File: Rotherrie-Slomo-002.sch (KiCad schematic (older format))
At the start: 8 parts, among them U2 TL074

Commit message: Oscillator section done
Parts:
- added C12, C17, C20: 100uF, symbol CP
- added C14, C16, C18, C19, C21, C22: 100nF, symbol C
- added R10, R11, R13, R14, R16, R6: 4.7k, symbol R
- added R12, R15, R8: 100k, symbol R
- added RV2, RV3, RV4: 500k, symbol POT
- added unit 3 of U2
- added unit 4 of U2
- added unit 2 of U2
- gave numbers to parts that had none: 7
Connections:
- net GND: now also C12.2, C14.1, C16.1, C17.2, C18.1, C19.1, C20.2, C21.1, C22.1, R11.2, R14.2, R6.2
- net VCC: now also C14.2, C18.2, C21.2, U2.4 (V+), U2.4 (V+), U2.4 (V+)
- net VEE: now also C16.2, C19.2, C22.2, U2.11 (V-), U2.11 (V-), U2.11 (V-)
- new net: R11.1, R13.2, U2.10 (+)
- new net: R13.1, U2.8
- new net: C17.1, R12.1, U2.9 (-)
- new net: R12.2, RV3.2, RV3.3
- new net: R14.1, R16.2, U2.12 (+)
- new net: C20.1, R15.1, U2.13 (-)
- new net: R16.1, U2.14
- new net: R15.2, RV4.2, RV4.3
- new net: R10.2, R6.1, U2.5 (+)
- new net: C12.1, R8.1, U2.6 (-)
- new net: R10.1, U2.7
- new net: R8.2, RV2.2, RV2.3
- new net WAVE2: RV3.1
- new net WAVE3: RV4.1
- new net WAVE4: RV2.1
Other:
- moved on the sheet: C11, C13, C15, R5, R7, R9, RV1, U2A

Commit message: Part associations made. 16pin connector reduced to 10 pin
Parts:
- removed C14, C16, C18, C19, C21, C22: 100nF, symbol C
- C10: renamed from C20; footprint (none) -> Capacitors_THT:CP_Radial_D7.5mm_P2.50mm
- C5: renamed from C11; footprint (none) -> Capacitors_THT:CP_Radial_D7.5mm_P2.50mm
- C6: renamed from C12; footprint (none) -> Capacitors_THT:CP_Radial_D7.5mm_P2.50mm
- C7: renamed from C13; footprint (none) -> Capacitors_THT:C_Disc_D4.3mm_W1.9mm_P5.00mm
- C8: renamed from C15; footprint (none) -> Capacitors_THT:C_Disc_D4.3mm_W1.9mm_P5.00mm
- C9: renamed from C17; footprint (none) -> Capacitors_THT:CP_Radial_D7.5mm_P2.50mm
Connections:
- net VCC: no longer U2.4 (V+), U2.4 (V+), U2.4 (V+)
- net VEE: no longer U2.11 (V-), U2.11 (V-), U2.11 (V-)
- net WAVE2: now also RV2.1; no longer RV3.1
- net WAVE3: now also RV3.1; no longer RV4.1
- net WAVE4: now also RV4.1; no longer RV2.1
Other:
- moved on the sheet: C6, R10, R6, R8, RV2, U2B

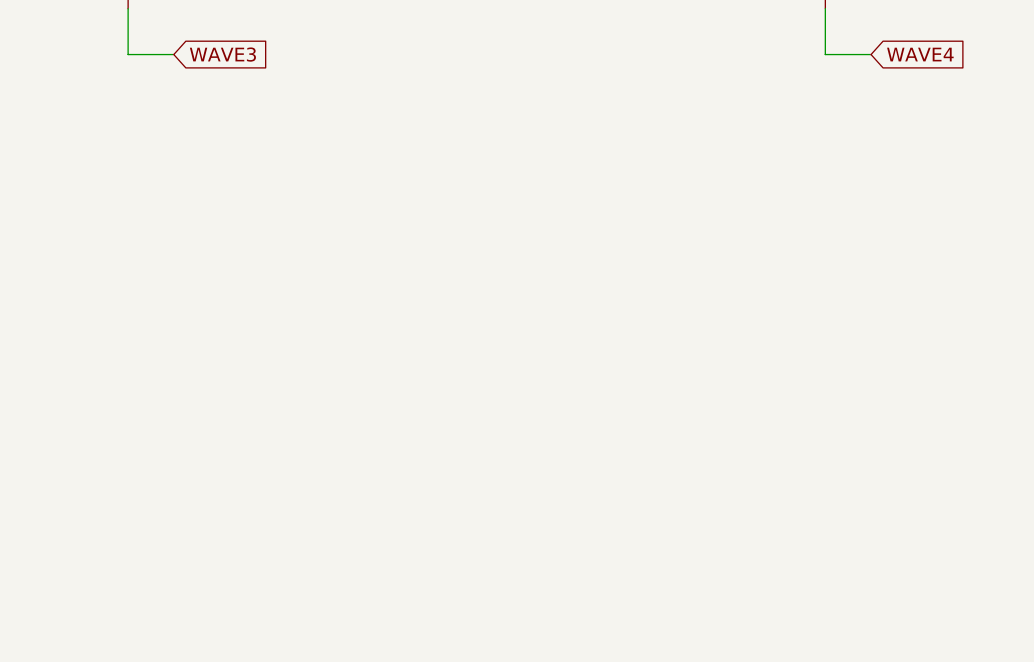
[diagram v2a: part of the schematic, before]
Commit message: Added jack connectors to schematic
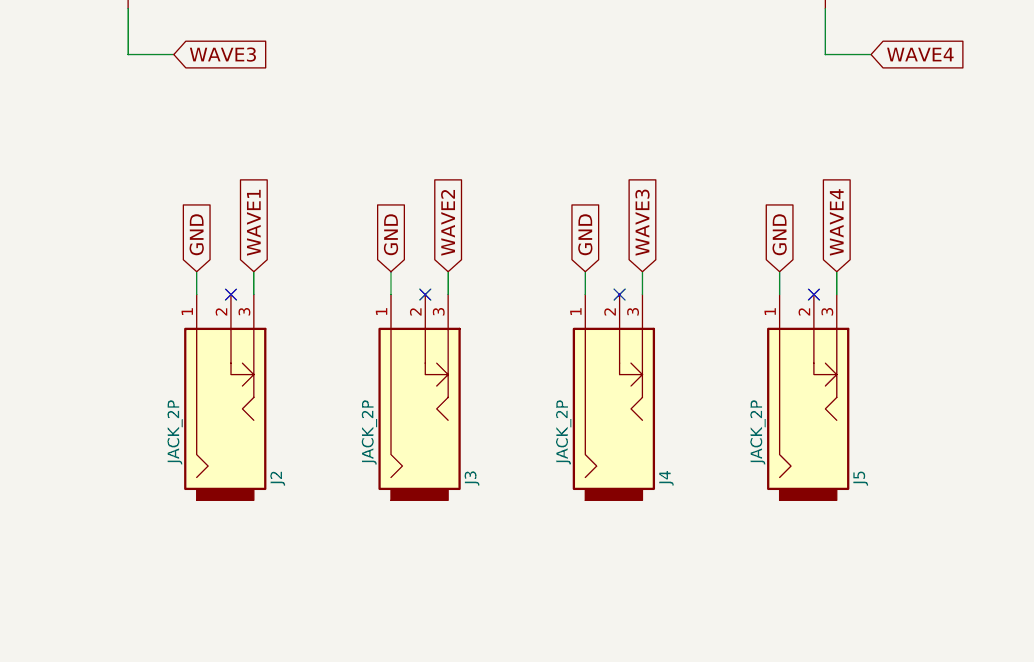
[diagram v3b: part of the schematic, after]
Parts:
- added J2, J3, J4, J5: JACK_2P, symbol JACK_2P
- R10, R11, R12, R13, R14, R15, R16, R5, R6, R7, R8, R9: footprint (none) -> Resistors_THT:R_Axial_DIN0207_L6.3mm_D2.5mm_P7.62mm_Horizontal
- RV1, RV2, RV3, RV4: footprint (none) -> Potentiometers:Potentiometer_Bourns_PTV09A-1_Horizontal
- U2: footprint (none) -> Housings_DIP:DIP-14_W7.62mm_Socket
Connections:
- net GND: now also J2.1, J3.1, J4.1, J5.1
- net WAVE1: now also J2.3
- net WAVE2: now also J3.3
- net WAVE3: now also J4.3
- net WAVE4: now also J5.3
- no-connect marks 0 -> 4
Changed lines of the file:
@@
 F 0 "U2" H 3350 2550 50  0000 L CNN
 F 1 "TL074" H 3350 2150 50  0000 L CNN
-F 2 "" H 3300 2450 50  0001 C CNN
+F 2 "Housings_DIP:DIP-14_W7.62mm_Socket" H 3300 2450 50  0001 C CNN
 F 3 "" H 3400 2550 50  0001 C CNN
 	1    3350 2350
@@
 F 0 "R9" V 3230 1350 50  0000 C CNN
 F 1 "4.7k" V 3150 1350 50  0000 C CNN
-F 2 "" V 3080 1350 50  0001 C CNN
+F 2 "Resistors_THT:R_Axial_DIN0207_L6.3mm_D2.5mm_P7.62mm_Horizontal" V 3080 1350 50  0001 C CNN
 F 3 "" H 3150 1350 50  0001 C CNN
 	1    3150 1350
@@
 F 0 "R5" V 2080 1350 50  0000 C CNN
 F 1 "4.7k" V 2000 1350 50  0000 C CNN
-F 2 "" V 1930 1350 50  0001 C CNN
+F 2 "Resistors_THT:R_Axial_DIN0207_L6.3mm_D2.5mm_P7.62mm_Horizontal" V 1930 1350 50  0001 C CNN
 F 3 "" H 2000 1350 50  0001 C CNN
 	1    2000 1350
@@
 F 0 "R7" V 2430 2900 50  0000 C CNN
 F 1 "100k" V 2350 2900 50  0000 C CNN
-F 2 "" V 2280 2900 50  0001 C CNN
+F 2 "Resistors_THT:R_Axial_DIN0207_L6.3mm_D2.5mm_P7.62mm_Horizontal" V 2280 2900 50  0001 C CNN
 F 3 "" H 2350 2900 50  0001 C CNN
 	1    2350 2900
@@
 F 0 "RV1" V 2325 3300 50  0000 C CNN
 F 1 "500k" V 2400 3300 50  0000 C CNN
-F 2 "" H 2500 3300 50  0001 C CNN
+F 2 "Potentiometers:Potentiometer_Bourns_PTV09A-1_Horizontal" H 2500 3300 50  0001 C CNN
 F 3 "" H 2500 3300 50  0001 C CNN
 	1    2500 3300
@@
 F 0 "U2" H 6400 2550 50  0000 L CNN
 F 1 "TL074" H 6400 2150 50  0000 L CNN
-F 2 "" H 6350 2450 50  0001 C CNN
+F 2 "Housings_DIP:DIP-14_W7.62mm_Socket" H 6350 2450 50  0001 C CNN
 F 3 "" H 6450 2550 50  0001 C CNN
 	3    6400 2350
@@
 F 0 "R13" V 6280 1350 50  0000 C CNN
 F 1 "4.7k" V 6200 1350 50  0000 C CNN
-F 2 "" V 6130 1350 50  0001 C CNN
+F 2 "Resistors_THT:R_Axial_DIN0207_L6.3mm_D2.5mm_P7.62mm_Horizontal" V 6130 1350 50  0001 C CNN
 F 3 "" H 6200 1350 50  0001 C CNN
 	1    6200 1350
@@
 F 0 "R11" V 5130 1350 50  0000 C CNN
 F 1 "4.7k" V 5050 1350 50  0000 C CNN
-F 2 "" V 4980 1350 50  0001 C CNN
+F 2 "Resistors_THT:R_Axial_DIN0207_L6.3mm_D2.5mm_P7.62mm_Horizontal" V 4980 1350 50  0001 C CNN
 F 3 "" H 5050 1350 50  0001 C CNN
 	1    5050 1350
@@
 F 0 "R12" V 5480 2900 50  0000 C CNN
 F 1 "100k" V 5400 2900 50  0000 C CNN
-F 2 "" V 5330 2900 50  0001 C CNN
+F 2 "Resistors_THT:R_Axial_DIN0207_L6.3mm_D2.5mm_P7.62mm_Horizontal" V 5330 2900 50  0001 C CNN
 F 3 "" H 5400 2900 50  0001 C CNN
 	1    5400 2900
@@
 F 0 "RV3" V 5375 3300 50  0000 C CNN
 F 1 "500k" V 5450 3300 50  0000 C CNN
-F 2 "" H 5550 3300 50  0001 C CNN
+F 2 "Potentiometers:Potentiometer_Bourns_PTV09A-1_Horizontal" H 5550 3300 50  0001 C CNN
 F 3 "" H 5550 3300 50  0001 C CNN
 	1    5550 3300
@@
 F 0 "U2" H 9450 2550 50  0000 L CNN
 F 1 "TL074" H 9450 2150 50  0000 L CNN
-F 2 "" H 9400 2450 50  0001 C CNN
+F 2 "Housings_DIP:DIP-14_W7.62mm_Socket" H 9400 2450 50  0001 C CNN
 F 3 "" H 9500 2550 50  0001 C CNN
 	4    9450 2350
@@
 F 0 "R16" V 9330 1350 50  0000 C CNN
 F 1 "4.7k" V 9250 1350 50  0000 C CNN
-F 2 "" V 9180 1350 50  0001 C CNN
+F 2 "Resistors_THT:R_Axial_DIN0207_L6.3mm_D2.5mm_P7.62mm_Horizontal" V 9180 1350 50  0001 C CNN
 F 3 "" H 9250 1350 50  0001 C CNN
 	1    9250 1350
@@
 F 0 "R14" V 8180 1350 50  0000 C CNN
 F 1 "4.7k" V 8100 1350 50  0000 C CNN
-F 2 "" V 8030 1350 50  0001 C CNN
+F 2 "Resistors_THT:R_Axial_DIN0207_L6.3mm_D2.5mm_P7.62mm_Horizontal" V 8030 1350 50  0001 C CNN
 F 3 "" H 8100 1350 50  0001 C CNN
 	1    8100 1350
@@
 F 0 "R15" V 8530 2900 50  0000 C CNN
 F 1 "100k" V 8450 2900 50  0000 C CNN
-F 2 "" V 8380 2900 50  0001 C CNN
+F 2 "Resistors_THT:R_Axial_DIN0207_L6.3mm_D2.5mm_P7.62mm_Horizontal" V 8380 2900 50  0001 C CNN
 F 3 "" H 8450 2900 50  0001 C CNN
 	1    8450 2900
@@
 F 0 "RV4" V 8425 3300 50  0000 C CNN
 F 1 "500k" V 8500 3300 50  0000 C CNN
-F 2 "" H 8600 3300 50  0001 C CNN
+F 2 "Potentiometers:Potentiometer_Bourns_PTV09A-1_Horizontal" H 8600 3300 50  0001 C CNN
 F 3 "" H 8600 3300 50  0001 C CNN
 	1    8600 3300
@@
 F 0 "U2" H 3350 5500 50  0000 L CNN
 F 1 "TL074" H 3350 5100 50  0000 L CNN
-F 2 "" H 3300 5400 50  0001 C CNN
+F 2 "Housings_DIP:DIP-14_W7.62mm_Socket" H 3300 5400 50  0001 C CNN
 F 3 "" H 3400 5500 50  0001 C CNN
 	2    3350 5300
@@
 F 0 "R10" V 3230 4300 50  0000 C CNN
 F 1 "4.7k" V 3150 4300 50  0000 C CNN
-F 2 "" V 3080 4300 50  0001 C CNN
+F 2 "Resistors_THT:R_Axial_DIN0207_L6.3mm_D2.5mm_P7.62mm_Horizontal" V 3080 4300 50  0001 C CNN
 F 3 "" H 3150 4300 50  0001 C CNN
 	1    3150 4300
@@
 F 0 "R6" V 2080 4300 50  0000 C CNN
 F 1 "4.7k" V 2000 4300 50  0000 C CNN
-F 2 "" V 1930 4300 50  0001 C CNN
+F 2 "Resistors_THT:R_Axial_DIN0207_L6.3mm_D2.5mm_P7.62mm_Horizontal" V 1930 4300 50  0001 C CNN
 F 3 "" H 2000 4300 50  0001 C CNN
 	1    2000 4300
@@
 F 0 "R8" V 2430 5850 50  0000 C CNN
 F 1 "100k" V 2350 5850 50  0000 C CNN
-F 2 "" V 2280 5850 50  0001 C CNN
+F 2 "Resistors_THT:R_Axial_DIN0207_L6.3mm_D2.5mm_P7.62mm_Horizontal" V 2280 5850 50  0001 C CNN
 F 3 "" H 2350 5850 50  0001 C CNN
 	1    2350 5850
@@
 F 0 "RV2" V 2325 6250 50  0000 C CNN
 F 1 "500k" V 2400 6250 50  0000 C CNN
-F 2 "" H 2500 6250 50  0001 C CNN
+F 2 "Potentiometers:Potentiometer_Bourns_PTV09A-1_Horizontal" H 2500 6250 50  0001 C CNN
 F 3 "" H 2500 6250 50  0001 C CNN
 	1    2500 6250
@@
 	2500 6050 2350 6050
 Connection ~ 2350 6050
+$Comp
+L JACK_2P J2
+U 1 1 59B2910B
+P 6000 5150
+F 0 "J2" H 5650 4950 50  0000 C CNN
+F 1 "JACK_2P" H 5850 5400 50  0000 C CNN
+F 2 "" H 6000 5150 50  0001 C CNN
+F 3 "" H 6000 5150 50  0001 C CNN
+	1    6000 5150
+	0    -1   -1   0
+$EndComp
+$Comp
+L JACK_2P J3
+U 1 1 59B291AD
+P 6850 5150
+F 0 "J3" H 6500 4950 50  0000 C CNN
+F 1 "JACK_2P" H 6700 5400 50  0000 C CNN
+F 2 "" H 6850 5150 50  0001 C CNN
+F 3 "" H 6850 5150 50  0001 C CNN
+	1    6850 5150
+	0    -1   -1   0
+$EndComp
+$Comp
+L JACK_2P J4
+U 1 1 59B29226
+P 7700 5150
+F 0 "J4" H 7350 4950 50  0000 C CNN
+F 1 "JACK_2P" H 7550 5400 50  0000 C CNN
+F 2 "" H 7700 5150 50  0001 C CNN
+F 3 "" H 7700 5150 50  0001 C CNN
+	1    7700 5150
+	0    -1   -1   0
+$EndComp
+$Comp
+L JACK_2P J5
+U 1 1 59B2929C
+P 8550 5150
+F 0 "J5" H 8200 4950 50  0000 C CNN
+F 1 "JACK_2P" H 8400 5400 50  0000 C CNN
+F 2 "" H 8550 5150 50  0001 C CNN
+F 3 "" H 8550 5150 50  0001 C CNN
+	1    8550 5150
+	0    -1   -1   0
+$EndComp
+Text GLabel 5850 4600 1    60   Input ~ 0
+GND
+Text GLabel 6700 4600 1    60   Input ~ 0
+GND
+Text GLabel 7550 4600 1    60   Input ~ 0
+GND
+Text GLabel 8400 4600 1    60   Input ~ 0
+GND
+Wire Wire Line
+	5850 4600 5850 4700
+Wire Wire Line
+	6700 4600 6700 4700
+Wire Wire Line
+	7550 4600 7550 4700
+Wire Wire Line
+	8400 4600 8400 4700
+Text GLabel 6100 4600 1    60   Input ~ 0
+WAVE1
+Text GLabel 6950 4600 1    60   Input ~ 0
+WAVE2
+Text GLabel 7800 4600 1    60   Input ~ 0
+WAVE3
+Text GLabel 8650 4600 1    60   Input ~ 0
+WAVE4
+Wire Wire Line
+	8650 4600 8650 4700
+Wire Wire Line
+	7800 4600 7800 4700
+Wire Wire Line
+	6950 4600 6950 4700
+Wire Wire Line
+	6100 4600 6100 4700
+NoConn ~ 6000 4700
+NoConn ~ 6850 4700
+NoConn ~ 7700 4700
+NoConn ~ 8550 4700
 $EndSCHEMATC

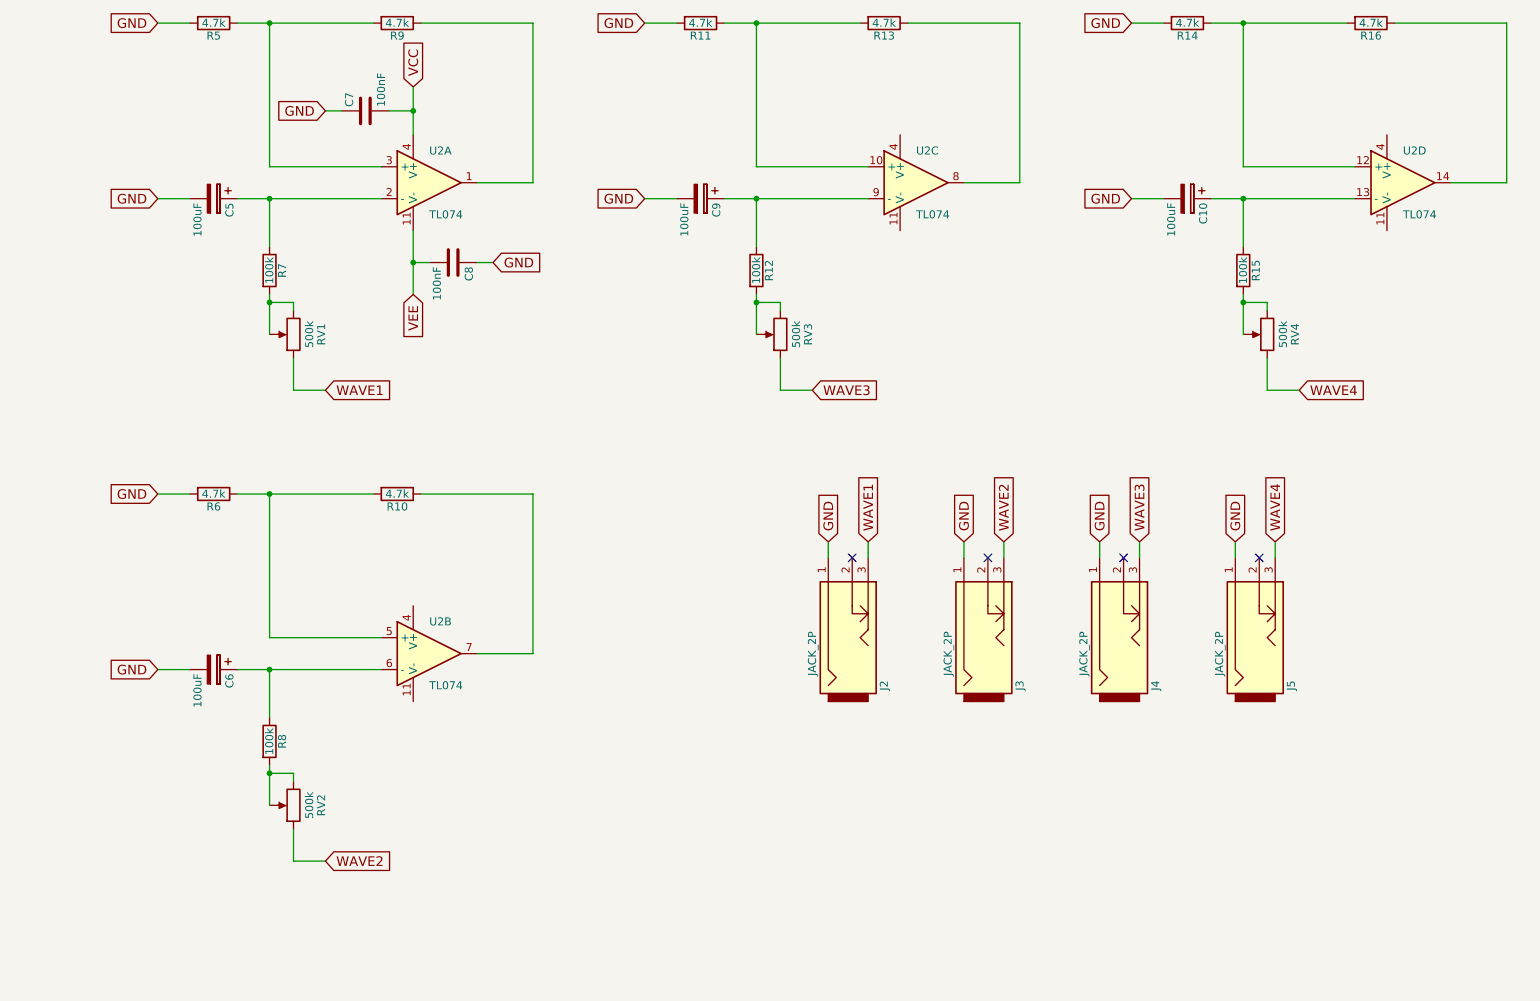
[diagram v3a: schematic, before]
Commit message: Rerouting from logic to controller board
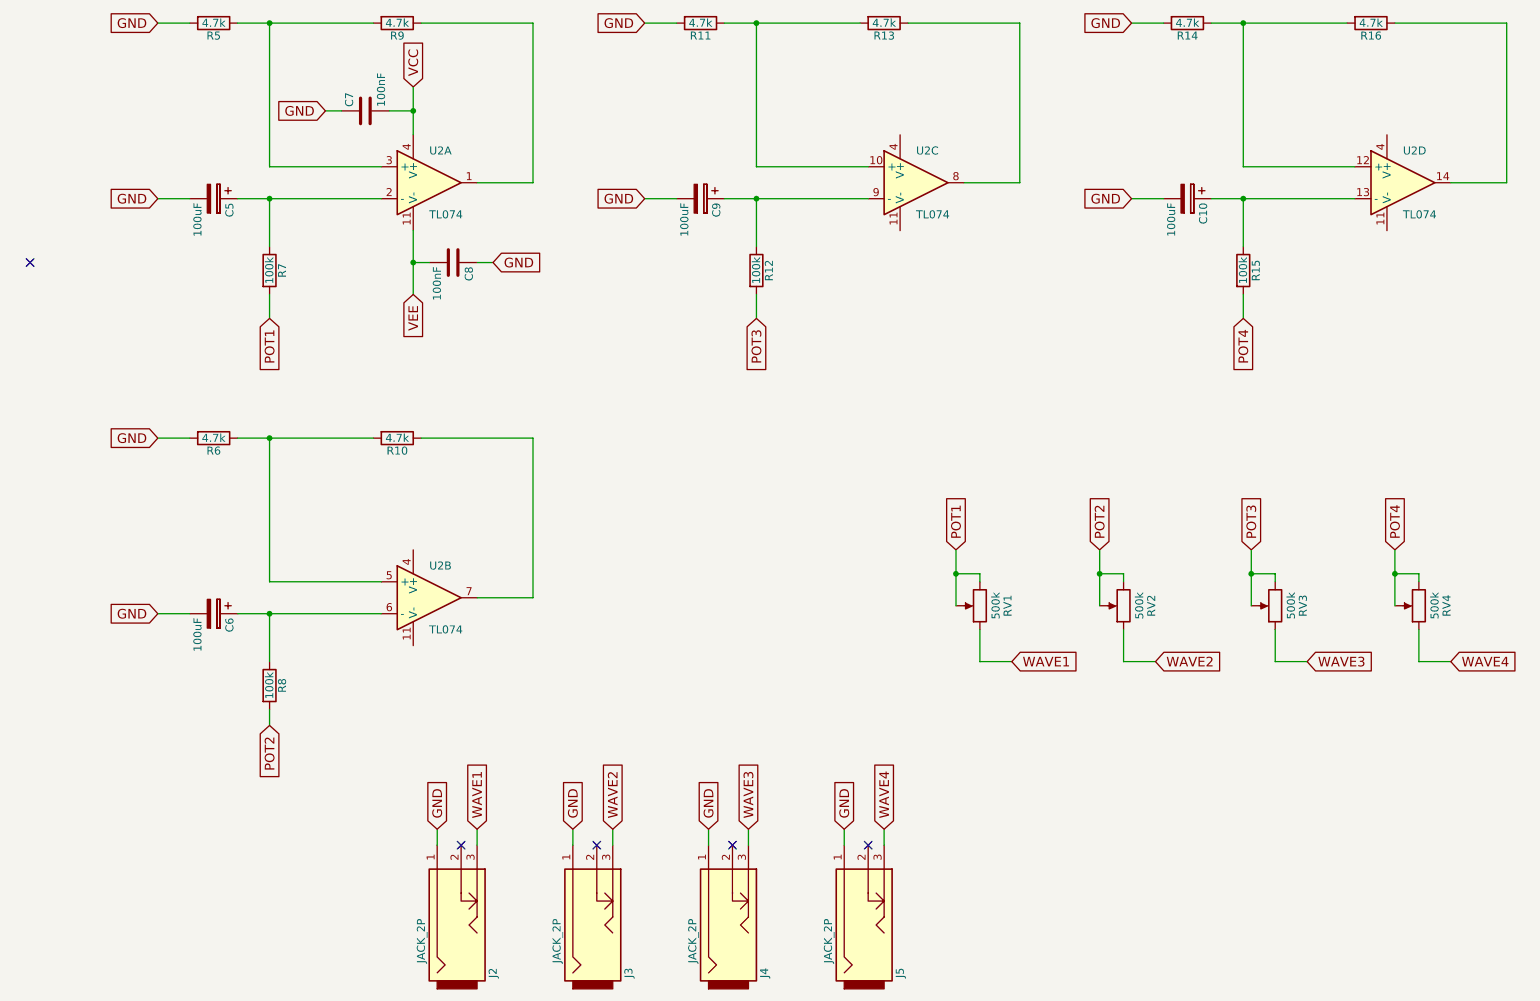
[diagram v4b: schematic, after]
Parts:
- J2, J3, J4, J5: footprint (none) -> Eurocad:PJ301M-12
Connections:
- net POT1: now reaches R7.2, RV1.2, RV1.3
- net POT3: now reaches R12.2, RV3.2, RV3.3
- net POT4: now reaches R15.2, RV4.2, RV4.3
- net POT2: now reaches R8.2, RV2.2, RV2.3
- no-connect marks 4 -> 5
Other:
- moved on the sheet: C6, J2, J3, J4, J5, R10, R6, R8, RV1, RV2, RV3, RV4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
